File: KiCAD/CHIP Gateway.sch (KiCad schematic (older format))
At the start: 9 parts, among them P1 CONN_01X02, P2 CONN_01X04, P3 CONN_01X04, U1 CHIP_Shield, U2 RFM69, U3 DS3231

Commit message: Ready for ordering
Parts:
- added P4, P5: CONN_01X05, Connectors_JST:JST_XH_S05B-XH-A_05x2.50mm_Angled, symbol CONN_01X05
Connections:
- net +3V3: now also P4.2 (P2), P5.2 (P2)
- net GND: now also P4.3 (P3), P5.3 (P3)
- net RX1: now also P4.5 (P5)
- net RX2: now also P5.5 (P5)
- net TX1: now also P4.4 (P4)
- net TX2: now also P5.4 (P4)
- net +5V: now reaches U1.3 (VCC-5V)
- net +5V: now also P4.1 (P1), P5.1 (P1)
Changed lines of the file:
@@
 Text GLabel 4350 4450 2    60   Input ~ 0
 RFM_INT
+$Comp
+L CONN_01X05 P5
+U 1 1 58A9A8E9
+P 6000 1400
+F 0 "P5" H 6000 1700 50  0000 C CNN
+F 1 "CONN_01X05" V 6100 1400 50  0000 C CNN
+F 2 "Connectors_JST:JST_XH_S05B-XH-A_05x2.50mm_Angled" H 6000 1400 50  0001 C CNN
+F 3 "" H 6000 1400 50  0000 C CNN
+	1    6000 1400
+	1    0    0    -1
+$EndComp
+$Comp
+L CONN_01X05 P4
+U 1 1 58A9AC7B
+P 4800 1400
+F 0 "P4" H 4800 1700 50  0000 C CNN
+F 1 "CONN_01X05" V 4900 1400 50  0000 C CNN
+F 2 "Connectors_JST:JST_XH_S05B-XH-A_05x2.50mm_Angled" H 4800 1400 50  0001 C CNN
+F 3 "" H 4800 1400 50  0000 C CNN
+	1    4800 1400
+	1    0    0    -1
+$EndComp
+$Comp
+L +5V #PWR011
+U 1 1 58A9ACED
+P 3150 2200
+F 0 "#PWR011" H 3150 2050 50  0001 C CNN
+F 1 "+5V" H 3150 2340 50  0000 C CNN
+F 2 "" H 3150 2200 50  0000 C CNN
+F 3 "" H 3150 2200 50  0000 C CNN
+	1    3150 2200
+	1    0    0    -1
+$EndComp
+$Comp
+L +5V #PWR012
+U 1 1 58A9ADF1
+P 4600 1200
+F 0 "#PWR012" H 4600 1050 50  0001 C CNN
+F 1 "+5V" H 4600 1340 50  0000 C CNN
+F 2 "" H 4600 1200 50  0000 C CNN
+F 3 "" H 4600 1200 50  0000 C CNN
+	1    4600 1200
+	1    0    0    -1
+$EndComp
+$Comp
+L +5V #PWR013
+U 1 1 58A9AEAA
+P 5800 1200
+F 0 "#PWR013" H 5800 1050 50  0001 C CNN
+F 1 "+5V" H 5800 1340 50  0000 C CNN
+F 2 "" H 5800 1200 50  0000 C CNN
+F 3 "" H 5800 1200 50  0000 C CNN
+	1    5800 1200
+	1    0    0    -1
+$EndComp
+$Comp
+L +3.3V #PWR014
+U 1 1 58A9AED6
+P 4450 1300
+F 0 "#PWR014" H 4450 1150 50  0001 C CNN
+F 1 "+3.3V" H 4450 1440 50  0000 C CNN
+F 2 "" H 4450 1300 50  0000 C CNN
+F 3 "" H 4450 1300 50  0000 C CNN
+	1    4450 1300
+	1    0    0    -1
+$EndComp
+$Comp
+L +3.3V #PWR015
+U 1 1 58A9AF02
+P 5650 1300
+F 0 "#PWR015" H 5650 1150 50  0001 C CNN
+F 1 "+3.3V" H 5650 1440 50  0000 C CNN
+F 2 "" H 5650 1300 50  0000 C CNN
+F 3 "" H 5650 1300 50  0000 C CNN
+	1    5650 1300
+	1    0    0    -1
+$EndComp
+Wire Wire Line
+	5650 1300 5800 1300
+Wire Wire Line
+	4450 1300 4600 1300
+$Comp
+L GND #PWR016
+U 1 1 58A9B046
+P 4450 1650
+F 0 "#PWR016" H 4450 1400 50  0001 C CNN
+F 1 "GND" H 4450 1500 50  0000 C CNN
+F 2 "" H 4450 1650 50  0000 C CNN
+F 3 "" H 4450 1650 50  0000 C CNN
+	1    4450 1650
+	1    0    0    -1
+$EndComp
+$Comp
+L GND #PWR017
+U 1 1 58A9B10C
+P 5650 1700
+F 0 "#PWR017" H 5650 1450 50  0001 C CNN
+F 1 "GND" H 5650 1550 50  0000 C CNN
+F 2 "" H 5650 1700 50  0000 C CNN
+F 3 "" H 5650 1700 50  0000 C CNN
+	1    5650 1700
+	1    0    0    -1
+$EndComp
+Wire Wire Line
+	5650 1700 5650 1400
+Wire Wire Line
+	5650 1400 5800 1400
+Wire Wire Line
+	4450 1650 4450 1400
+Wire Wire Line
+	4450 1400 4600 1400
+Text GLabel 4350 1500 0    60   Input ~ 0
+TX1
+Text GLabel 4350 1600 0    60   Input ~ 0
+RX1
+Text GLabel 5550 1500 0    60   Input ~ 0
+TX2
+Text GLabel 5550 1600 0    60   Input ~ 0
+RX2
+Wire Wire Line
+	5550 1600 5800 1600
+Wire Wire Line
+	5800 1500 5550 1500
+Wire Wire Line
+	4600 1500 4350 1500
+Wire Wire Line
+	4350 1600 4600 1600
 $EndSCHEMATC

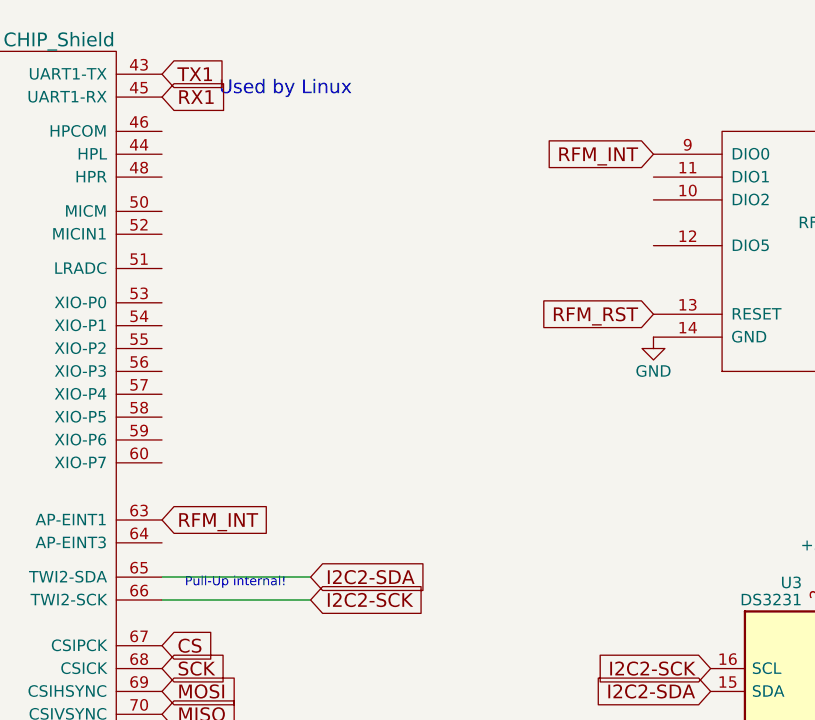
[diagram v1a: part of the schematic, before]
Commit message: Connected DIO1
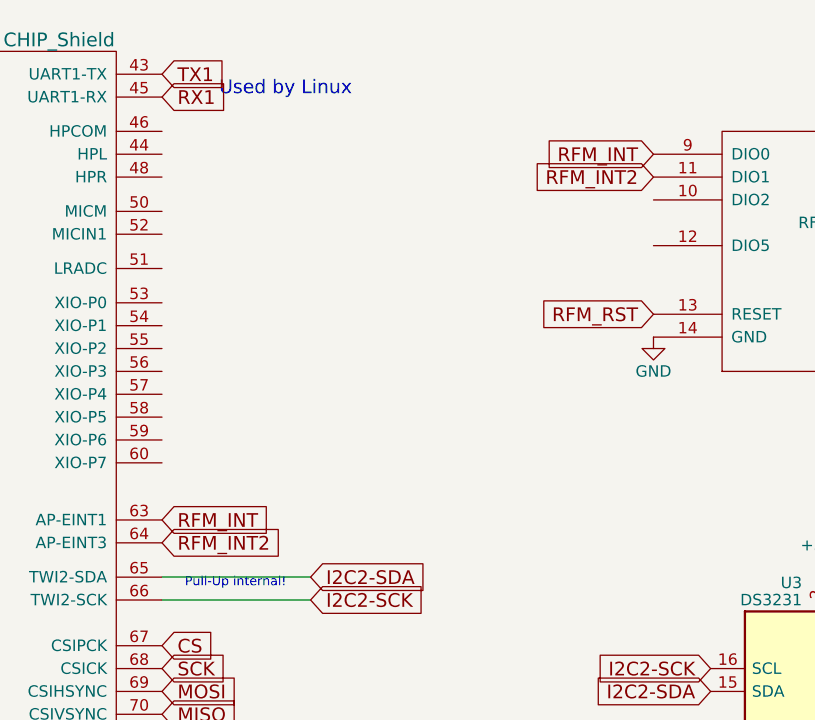
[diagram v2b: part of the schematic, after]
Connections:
- net RFM_INT2: now reaches U1.64 (AP-EINT3)
- net RFM_INT2: now also U2.11 (DIO1)
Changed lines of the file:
@@
 Wire Wire Line
 	4350 1600 4600 1600
+Text GLabel 6500 2950 0    60   Input ~ 0
+RFM_INT2
+Text GLabel 4350 4550 2    60   Input ~ 0
+RFM_INT2
 $EndSCHEMATC
